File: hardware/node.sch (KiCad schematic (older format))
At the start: 2 parts, among them U1 NRF24L01_Breakout, U2 BluePill_STM32F103C

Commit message: Differentail control
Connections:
- net PB8: now reaches U2.36 (PB8)
- net PB9: now reaches U2.37 (PB9)
- no-connect marks 23 -> 24
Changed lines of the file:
@@
 	6900 3250 6900 2300
 $Comp
-L power:+5V #PWR?
+L power:+5V #PWR0123
 U 1 1 5C13D36B
 P 6900 2300
-F 0 "#PWR?" H 6900 2150 50  0001 C CNN
+F 0 "#PWR0123" H 6900 2150 50  0001 C CNN
 F 1 "+5V" H 6915 2473 50  0000 C CNN
 F 2 "" H 6900 2300 50  0001 C CNN
@@
 	1    0    0    -1
 $EndComp
+Wire Wire Line
+	6550 3350 7250 3350
+Wire Wire Line
+	6550 3450 7250 3450
+Text HLabel 7250 3450 2    50   Output ~ 0
+PB8
+Text HLabel 7250 3350 2    50   Output ~ 0
+PB9
+NoConn ~ 6550 3150
 $EndSCHEMATC

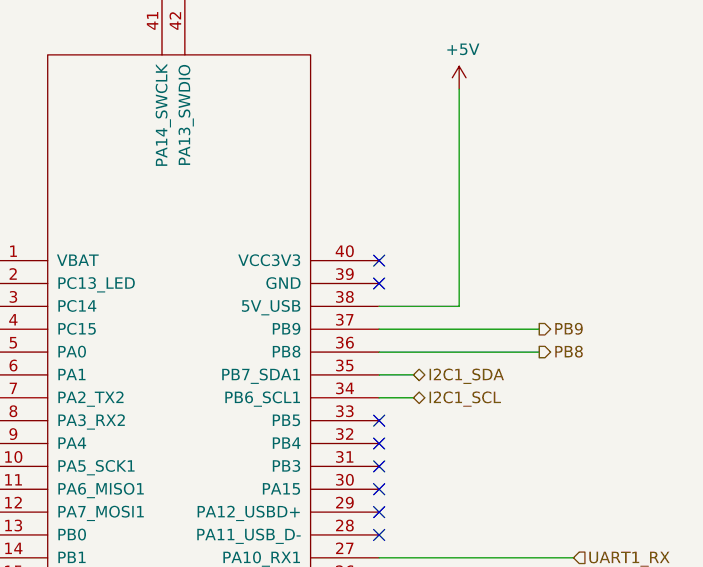
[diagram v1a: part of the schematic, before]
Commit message: Add onboard temp sensor
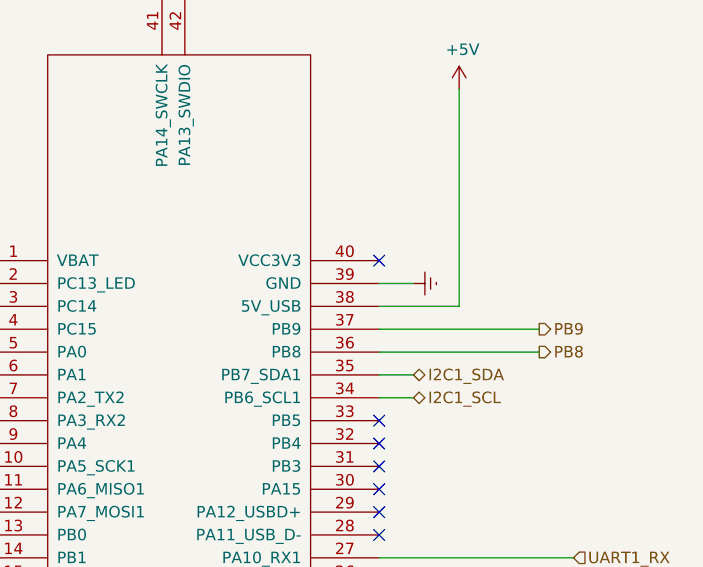
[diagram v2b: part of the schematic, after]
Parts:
- U2: footprint BLUEPILL -> DIP40
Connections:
- net GNDREF: now also U2.39 (GND)
- no-connect marks 24 -> 23
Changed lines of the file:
@@
 F 0 "U2" H 5675 2278 50  0000 C CNN
 F 1 "BluePill_STM32F103C" H 5675 2187 50  0000 C CNN
-F 2 "BLUEPILL" H 5700 2150 50  0001 C CNN
+F 2 "DIP40" H 5700 2150 50  0001 C CNN
 F 3 "www.rogerclark.net" H 5650 2250 50  0001 C CNN
 	1    5650 3750
@@
 Text HLabel 7250 3350 2    50   Output ~ 0
 PB9
-NoConn ~ 6550 3150
+$Comp
+L power:GNDREF #PWR?
+U 1 1 5C16DC3A
+P 6700 3150
+AR Path="/5C16DC3A" Ref="#PWR?"  Part="1"
+AR Path="/5C14BAF9/5C16DC3A" Ref="#PWR?"  Part="1"
+F 0 "#PWR?" H 6700 2900 50  0001 C CNN
+F 1 "GNDREF" H 6705 2977 50  0001 C CNN
+F 2 "" H 6700 3150 50  0001 C CNN
+F 3 "" H 6700 3150 50  0001 C CNN
+	1    6700 3150
+	0    -1   -1   0
+$EndComp
+Wire Wire Line
+	6700 3150 6550 3150
 $EndSCHEMATC

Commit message: Set point set with terminal
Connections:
- net labels added: ONBOARD_LM335
- wire segments 24 -> 25
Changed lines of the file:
@@
 Wire Wire Line
 	6700 3150 6550 3150
+Wire Wire Line
+	3100 3650 4800 3650
+Text Label 3300 3650 0    50   ~ 0
+ONBOARD_LM335
 $EndSCHEMATC
